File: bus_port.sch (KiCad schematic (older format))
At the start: 2 parts, among them P1 CONN_01X40, P5 CONN_01X04

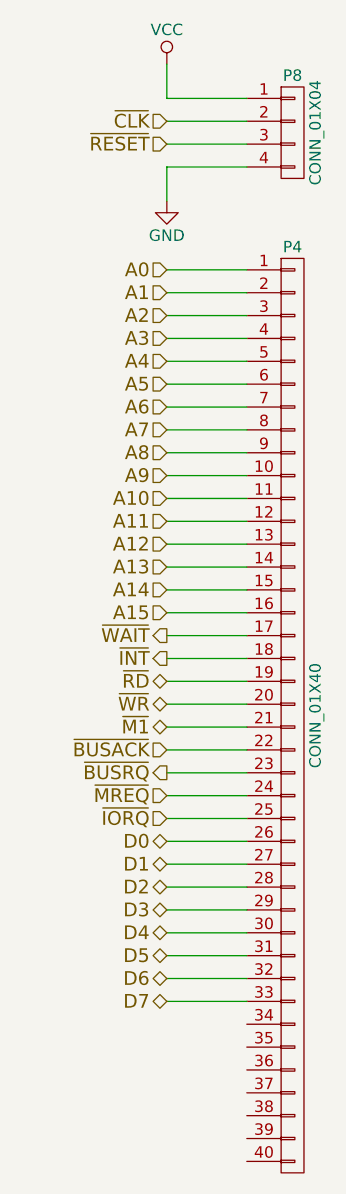
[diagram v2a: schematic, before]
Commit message: More card slot clean up. Added NMI signal for DMA
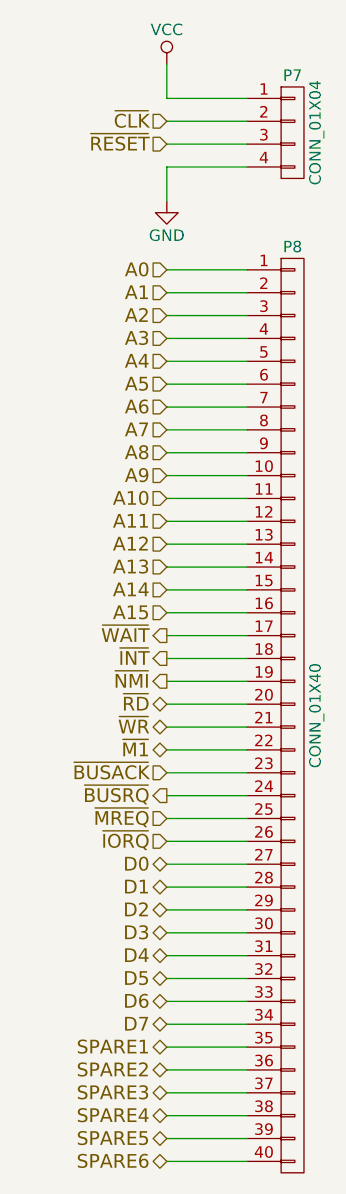
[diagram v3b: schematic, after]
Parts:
- renumbered P5 to P1
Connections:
- net D0: now also P1.27 (P27); no longer P1.26 (P26)
- net D1: now also P1.28 (P28); no longer P1.27 (P27)
- net D2: now also P1.29 (P29); no longer P1.28 (P28)
- net D3: now also P1.30 (P30); no longer P1.29 (P29)
- net D4: now also P1.31 (P31); no longer P1.30 (P30)
- net D5: now also P1.32 (P32); no longer P1.31 (P31)
- net D6: now also P1.33 (P33); no longer P1.32 (P32)
- net D7: now also P1.34 (P34); no longer P1.33 (P33)
- net ~BUSACK: now also P1.23 (P23); no longer P1.22 (P22)
- net ~BUSRQ: now also P1.24 (P24); no longer P1.23 (P23)
- net ~IORQ: now also P1.26 (P26); no longer P1.25 (P25)
- net ~M1: now also P1.22 (P22); no longer P1.21 (P21)
- net ~MREQ: now also P1.25 (P25); no longer P1.24 (P24)
- net ~RD: now also P1.20 (P20); no longer P1.19 (P19)
- net ~WR: now also P1.21 (P21); no longer P1.20 (P20)
- net SPARE1: now reaches P1.35 (P35)
- net SPARE2: now reaches P1.36 (P36)
- net SPARE3: now reaches P1.37 (P37)
- net SPARE4: now reaches P1.38 (P38)
- net SPARE5: now reaches P1.39 (P39)
- net SPARE6: now reaches P1.40 (P40)
- new net ~NMI: P1.19 (P19)
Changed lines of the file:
@@
 $Descr A4 11693 8268
 encoding utf-8
-Sheet 4 7
+Sheet 7 7
 Title ""
 Date ""
@@
 Text HLabel 3550 3650 0    60   Input ~ 0
 A15
-Text HLabel 3550 4650 0    60   3State ~ 0
+Text HLabel 3550 4750 0    60   3State ~ 0
 D0
-Text HLabel 3550 4750 0    60   3State ~ 0
+Text HLabel 3550 4850 0    60   3State ~ 0
 D1
-Text HLabel 3550 4850 0    60   3State ~ 0
+Text HLabel 3550 4950 0    60   3State ~ 0
 D2
-Text HLabel 3550 4950 0    60   3State ~ 0
+Text HLabel 3550 5050 0    60   3State ~ 0
 D3
-Text HLabel 3550 5050 0    60   3State ~ 0
+Text HLabel 3550 5150 0    60   3State ~ 0
 D4
-Text HLabel 3550 5150 0    60   3State ~ 0
+Text HLabel 3550 5250 0    60   3State ~ 0
 D5
-Text HLabel 3550 5250 0    60   3State ~ 0
+Text HLabel 3550 5350 0    60   3State ~ 0
 D6
-Text HLabel 3550 5350 0    60   3State ~ 0
+Text HLabel 3550 5450 0    60   3State ~ 0
 D7
 Text HLabel 3550 3750 0    60   Output ~ 0
@@
 Text HLabel 3550 3850 0    60   Output ~ 0
 ~INT
-Text HLabel 3550 3950 0    60   3State ~ 0
+Text HLabel 3550 4050 0    60   3State ~ 0
 ~RD
-Text HLabel 3550 4050 0    60   3State ~ 0
+Text HLabel 3550 4150 0    60   3State ~ 0
 ~WR
-Text HLabel 3550 4150 0    60   3State ~ 0
+Text HLabel 3550 4250 0    60   3State ~ 0
 ~M1
-Text HLabel 3550 4250 0    60   Input ~ 0
+Text HLabel 3550 4350 0    60   Input ~ 0
 ~BUSACK
-Text HLabel 3550 4350 0    60   Output ~ 0
+Text HLabel 3550 4450 0    60   Output ~ 0
 ~BUSRQ
-Text HLabel 3550 4450 0    60   Input ~ 0
+Text HLabel 3550 4550 0    60   Input ~ 0
 ~MREQ
-Text HLabel 3550 4550 0    60   Input ~ 0
+Text HLabel 3550 4650 0    60   Input ~ 0
 ~IORQ
 $Comp
@@
 AR Path="/577BB11C/577CEB68" Ref="P1"  Part="1"
 AR Path="/577C4BD1/577CEB68" Ref="P2"  Part="1"
-AR Path="/577F17CE/577F1897/577CEB68" Ref="P1"  Part="1"
+AR Path="/577F17CE/577F1897/577CEB68" Ref="P2"  Part="1"
 AR Path="/577F17CE/577F7EB3/577CEB68" Ref="P2"  Part="1"
 AR Path="/577F17CE/577F8AF5/577CEB68" Ref="P3"  Part="1"
 AR Path="/577F17CE/577F9440/577CEB68" Ref="P4"  Part="1"
-F 0 "P4" H 4100 6150 50  0000 C CNN
+AR Path="/577F17CE/5782F6B6/577CEB68" Ref="P4"  Part="1"
+AR Path="/577F17CE/5783136E/577CEB68" Ref="P6"  Part="1"
+AR Path="/577F17CE/57832B70/577CEB68" Ref="P8"  Part="1"
+F 0 "P8" H 4100 6150 50  0000 C CNN
 F 1 "CONN_01X40" V 4200 4100 50  0000 C CNN
 F 2 "Socket_Strips:Socket_Strip_Straight_1x40" H 4100 4100 50  0001 C CNN
@@
 	3550 3650 3900 3650
 Wire Wire Line
+	3550 4750 3900 4750
+Wire Wire Line
+	3550 4850 3900 4850
+Wire Wire Line
+	3550 4950 3900 4950
+Wire Wire Line
+	3550 5050 3900 5050
+Wire Wire Line
+	3550 5150 3900 5150
+Wire Wire Line
+	3550 5250 3900 5250
+Wire Wire Line
+	3550 5350 3900 5350
+Wire Wire Line
+	3550 5450 3900 5450
+Wire Wire Line
+	3550 3750 3900 3750
+Wire Wire Line
+	3550 3850 3900 3850
+Wire Wire Line
+	3550 4050 3900 4050
+Wire Wire Line
+	3550 4150 3900 4150
+Wire Wire Line
+	3550 4250 3900 4250
+Wire Wire Line
+	3550 4350 3900 4350
+Wire Wire Line
+	3550 4450 3900 4450
+Wire Wire Line
+	3550 4550 3900 4550
+Wire Wire Line
 	3550 4650 3900 4650
-Wire Wire Line
-	3550 4750 3900 4750
-Wire Wire Line
-	3550 4850 3900 4850
-Wire Wire Line
-	3550 4950 3900 4950
-Wire Wire Line
-	3550 5050 3900 5050
-Wire Wire Line
-	3550 5150 3900 5150
-Wire Wire Line
-	3550 5250 3900 5250
-Wire Wire Line
-	3550 5350 3900 5350
-Wire Wire Line
-	3550 3750 3900 3750
-Wire Wire Line
-	3550 3850 3900 3850
-Wire Wire Line
-	3550 3950 3900 3950
-Wire Wire Line
-	3550 4050 3900 4050
-Wire Wire Line
-	3550 4150 3900 4150
-Wire Wire Line
-	3550 4250 3900 4250
-Wire Wire Line
-	3550 4350 3900 4350
-Wire Wire Line
-	3550 4450 3900 4450
-Wire Wire Line
-	3550 4550 3900 4550
 Text HLabel 3550 1500 0    60   Input ~ 0
 ~CLK
 $Comp
-L CONN_01X04 P5
+L CONN_01X04 P1
 U 1 1 578144F7
 P 4100 1550
-AR Path="/577F17CE/577F1897/578144F7" Ref="P5"  Part="1"
+AR Path="/577F17CE/577F1897/578144F7" Ref="P1"  Part="1"
 AR Path="/577F17CE/577F7EB3/578144F7" Ref="P6"  Part="1"
 AR Path="/577F17CE/577F8AF5/578144F7" Ref="P7"  Part="1"
 AR Path="/577F17CE/577F9440/578144F7" Ref="P8"  Part="1"
-F 0 "P8" H 4100 1800 50  0000 C CNN
+AR Path="/577F17CE/5782F6B6/578144F7" Ref="P3"  Part="1"
+AR Path="/577F17CE/5783136E/578144F7" Ref="P5"  Part="1"
+AR Path="/577F17CE/57832B70/578144F7" Ref="P7"  Part="1"
+F 0 "P7" H 4100 1800 50  0000 C CNN
 F 1 "CONN_01X04" V 4200 1550 50  0000 C CNN
 F 2 "" H 4100 1550 50  0000 C CNN
@@
 AR Path="/577F17CE/577F8AF5/5781454A" Ref="#PWR021"  Part="1"
 AR Path="/577F17CE/577F9440/5781454A" Ref="#PWR023"  Part="1"
+AR Path="/577F17CE/5782F6B6/5781454A" Ref="#PWR019"  Part="1"
+AR Path="/577F17CE/5783136E/5781454A" Ref="#PWR021"  Part="1"
+AR Path="/577F17CE/57832B70/5781454A" Ref="#PWR023"  Part="1"
 F 0 "#PWR023" H 3550 1100 50  0001 C CNN
 F 1 "VCC" H 3550 1400 50  0000 C CNN
@@
 AR Path="/577F17CE/577F8AF5/5781458A" Ref="#PWR022"  Part="1"
 AR Path="/577F17CE/577F9440/5781458A" Ref="#PWR024"  Part="1"
+AR Path="/577F17CE/5782F6B6/5781458A" Ref="#PWR020"  Part="1"
+AR Path="/577F17CE/5783136E/5781458A" Ref="#PWR022"  Part="1"
+AR Path="/577F17CE/57832B70/5781458A" Ref="#PWR024"  Part="1"
 F 0 "#PWR024" H 3550 1600 50  0001 C CNN
 F 1 "GND" H 3550 1700 50  0000 C CNN
@@
 Text HLabel 3550 1600 0    60   Input ~ 0
 ~RESET
+Wire Wire Line
+	3900 3950 3550 3950
+Text HLabel 3550 3950 0    60   Output ~ 0
+~NMI
+Wire Wire Line
+	3900 5550 3550 5550
+Wire Wire Line
+	3900 5650 3550 5650
+Wire Wire Line
+	3900 5750 3550 5750
+Wire Wire Line
+	3900 5850 3550 5850
+Wire Wire Line
+	3900 5950 3550 5950
+Wire Wire Line
+	3900 6050 3550 6050
+Text HLabel 3550 5550 0    60   BiDi ~ 0
+SPARE1
+Text HLabel 3550 5650 0    60   BiDi ~ 0
+SPARE2
+Text HLabel 3550 5750 0    60   BiDi ~ 0
+SPARE3
+Text HLabel 3550 5850 0    60   BiDi ~ 0
+SPARE4
+Text HLabel 3550 5950 0    60   BiDi ~ 0
+SPARE5
+Text HLabel 3550 6050 0    60   BiDi ~ 0
+SPARE6
 $EndSCHEMATC

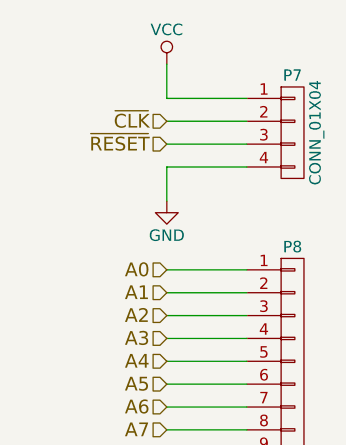
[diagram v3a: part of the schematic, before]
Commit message: Added IO sheet, fixed pin types to match z80
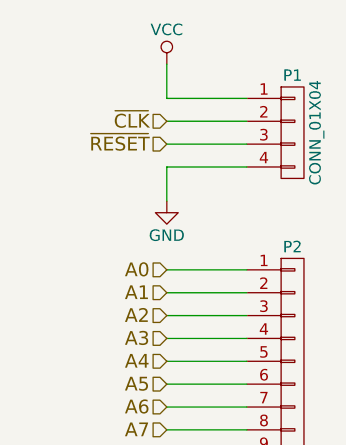
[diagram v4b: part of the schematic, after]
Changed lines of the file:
@@
 $Descr A4 11693 8268
 encoding utf-8
-Sheet 7 7
+Sheet 4 8
 Title ""
 Date ""
@@
 AR Path="/577F17CE/5783136E/577CEB68" Ref="P6"  Part="1"
 AR Path="/577F17CE/57832B70/577CEB68" Ref="P8"  Part="1"
-F 0 "P8" H 4100 6150 50  0000 C CNN
+F 0 "P2" H 4100 6150 50  0000 C CNN
 F 1 "CONN_01X40" V 4200 4100 50  0000 C CNN
 F 2 "Socket_Strips:Socket_Strip_Straight_1x40" H 4100 4100 50  0001 C CNN
@@
 AR Path="/577F17CE/5783136E/578144F7" Ref="P5"  Part="1"
 AR Path="/577F17CE/57832B70/578144F7" Ref="P7"  Part="1"
-F 0 "P7" H 4100 1800 50  0000 C CNN
+F 0 "P1" H 4100 1800 50  0000 C CNN
 F 1 "CONN_01X04" V 4200 1550 50  0000 C CNN
 F 2 "" H 4100 1550 50  0000 C CNN
@@
 AR Path="/577F17CE/5783136E/5781454A" Ref="#PWR021"  Part="1"
 AR Path="/577F17CE/57832B70/5781454A" Ref="#PWR023"  Part="1"
-F 0 "#PWR023" H 3550 1100 50  0001 C CNN
+F 0 "#PWR017" H 3550 1100 50  0001 C CNN
 F 1 "VCC" H 3550 1400 50  0000 C CNN
 F 2 "" H 3550 1250 50  0000 C CNN
@@
 AR Path="/577F17CE/5783136E/5781458A" Ref="#PWR022"  Part="1"
 AR Path="/577F17CE/57832B70/5781458A" Ref="#PWR024"  Part="1"
-F 0 "#PWR024" H 3550 1600 50  0001 C CNN
+F 0 "#PWR018" H 3550 1600 50  0001 C CNN
 F 1 "GND" H 3550 1700 50  0000 C CNN
 F 2 "" H 3550 1850 50  0000 C CNN

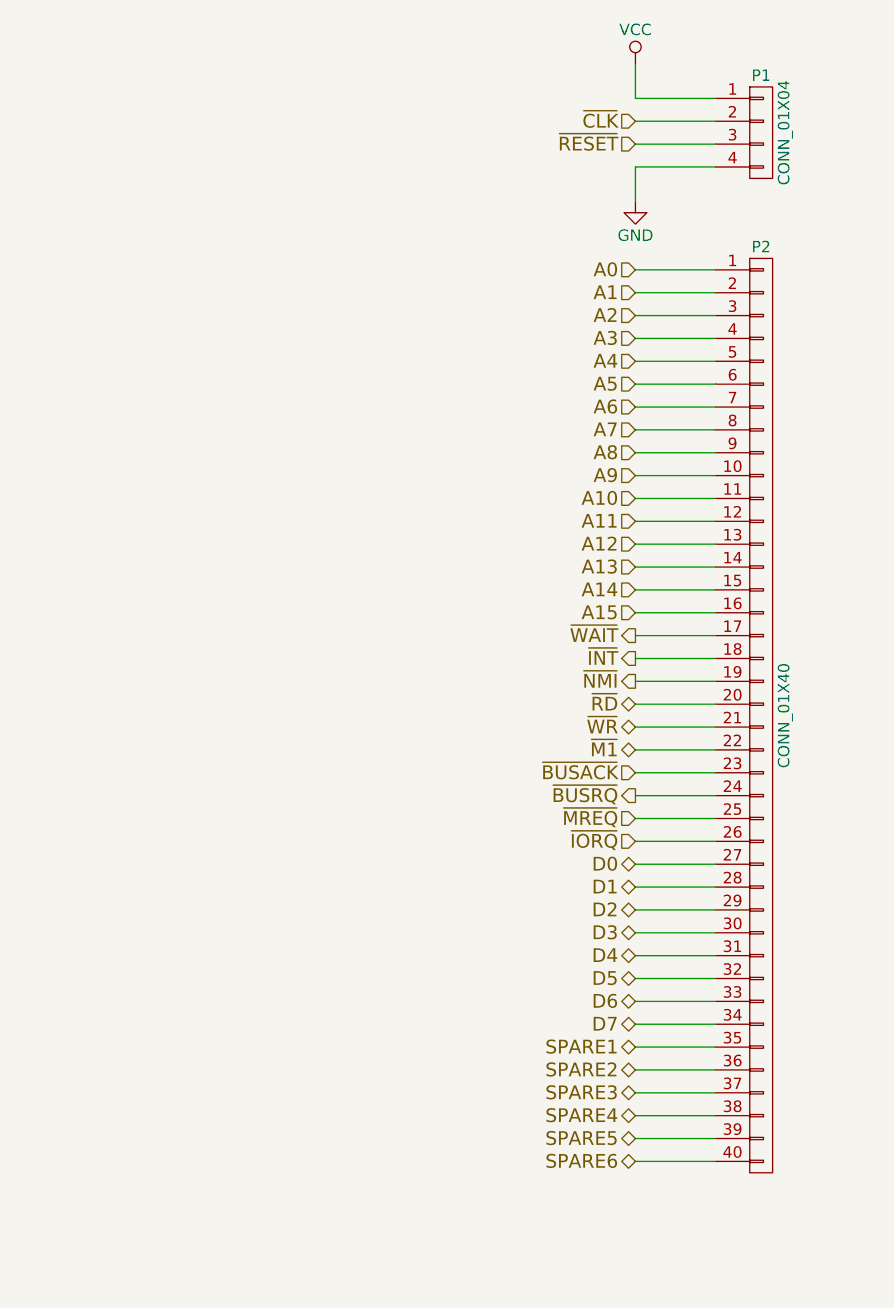
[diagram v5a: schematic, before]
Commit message: Added missing signals to IO and added buffer
I've removed the /WAIT and also added a somewhat dodgy diode AND to
handle the bi-directional Dx buffer. Might work, might not.

Also cleaned up the buses and just tidied things up.
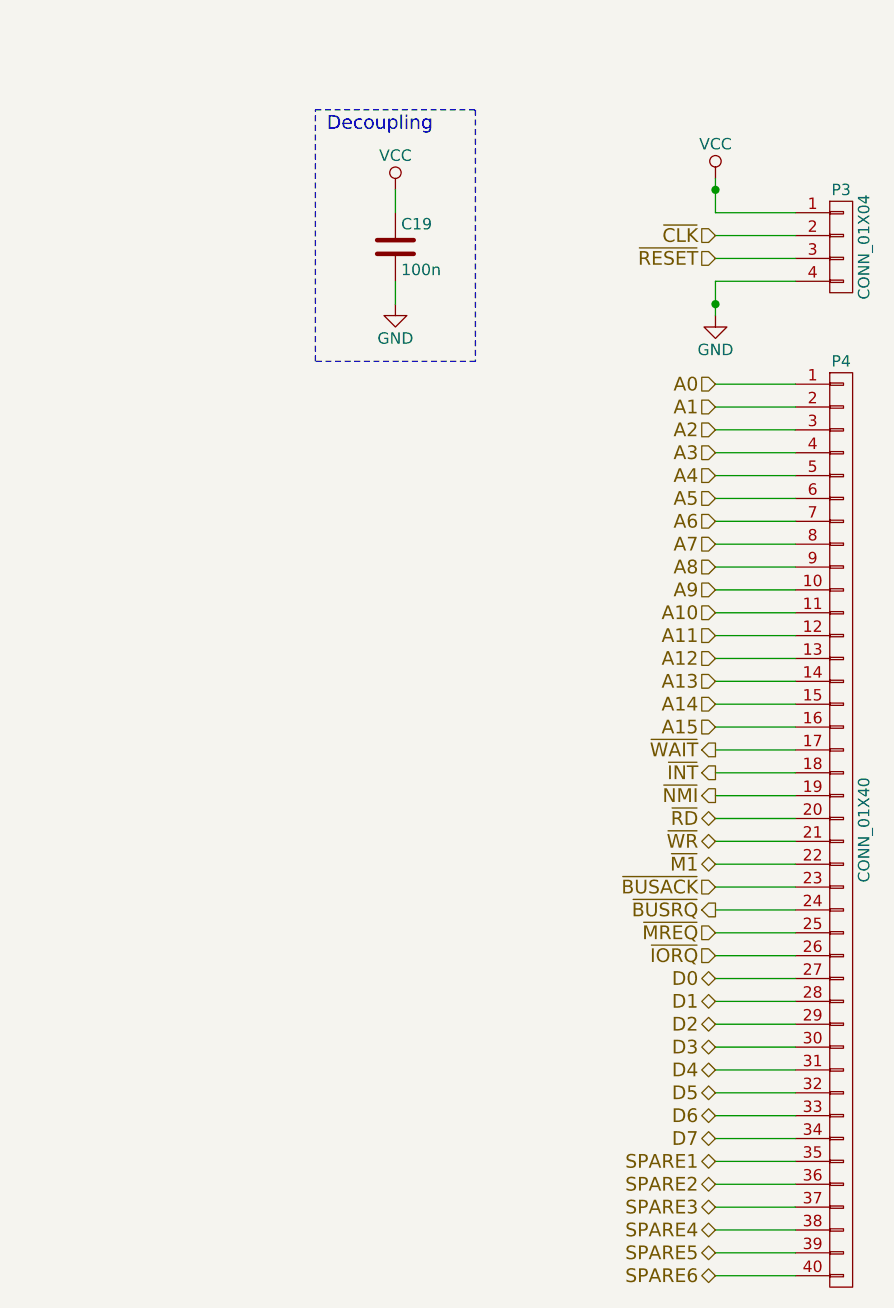
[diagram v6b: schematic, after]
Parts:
- added C18: 100n, symbol C
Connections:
- net GND: now also C18.2
- net VCC: now also C18.1
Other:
- note added: "Decoupling"
- moved on the sheet: P3, P4
